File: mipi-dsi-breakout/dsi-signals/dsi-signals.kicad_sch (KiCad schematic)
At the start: 19 parts, among them J1 Conn_01x03_Pin, J2 Conn_01x06_Pin, J5 Conn_01x01_Pin

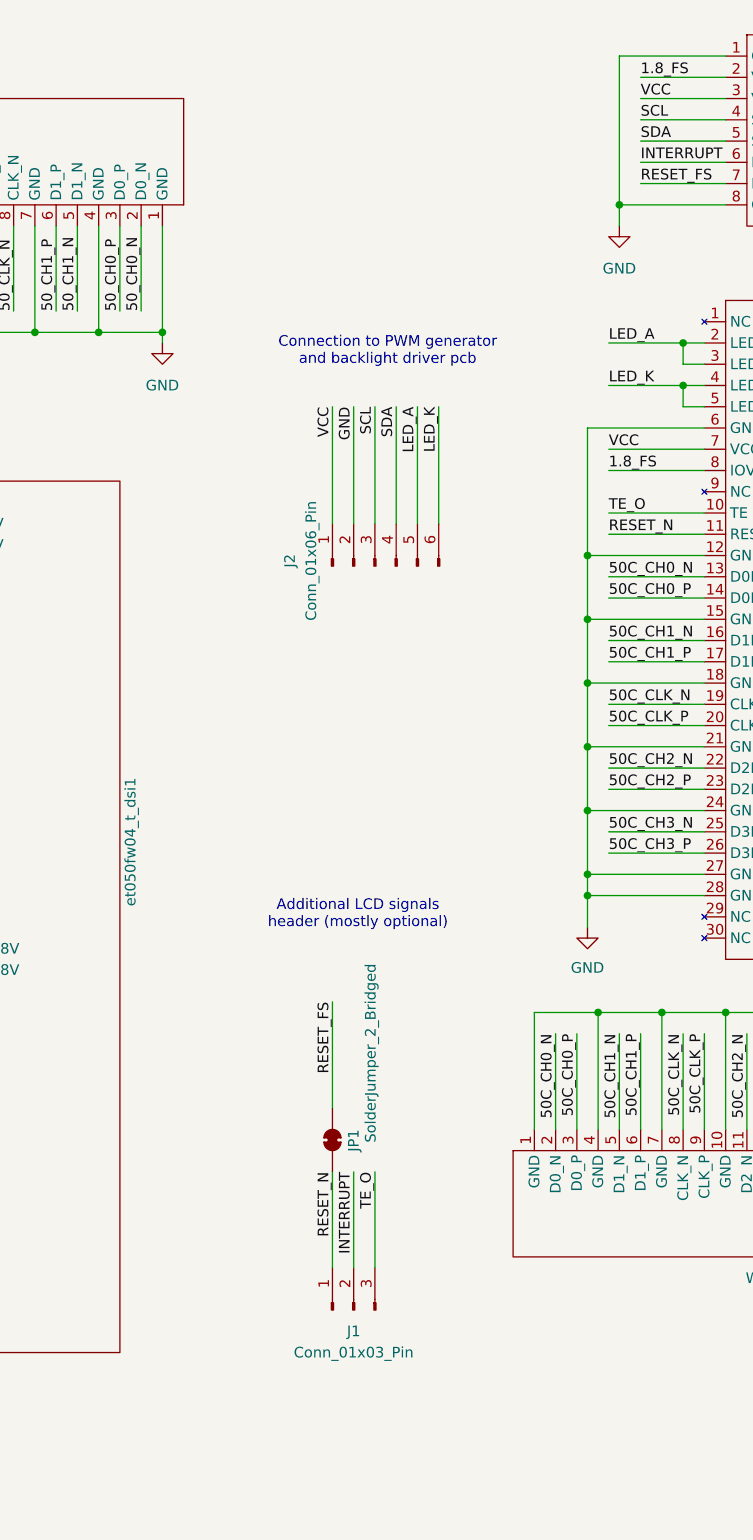
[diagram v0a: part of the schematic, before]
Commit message: Add SUS grounding to dsi-signals. Add lcd-peripherals.
To the mipi-dsi-breakout project.
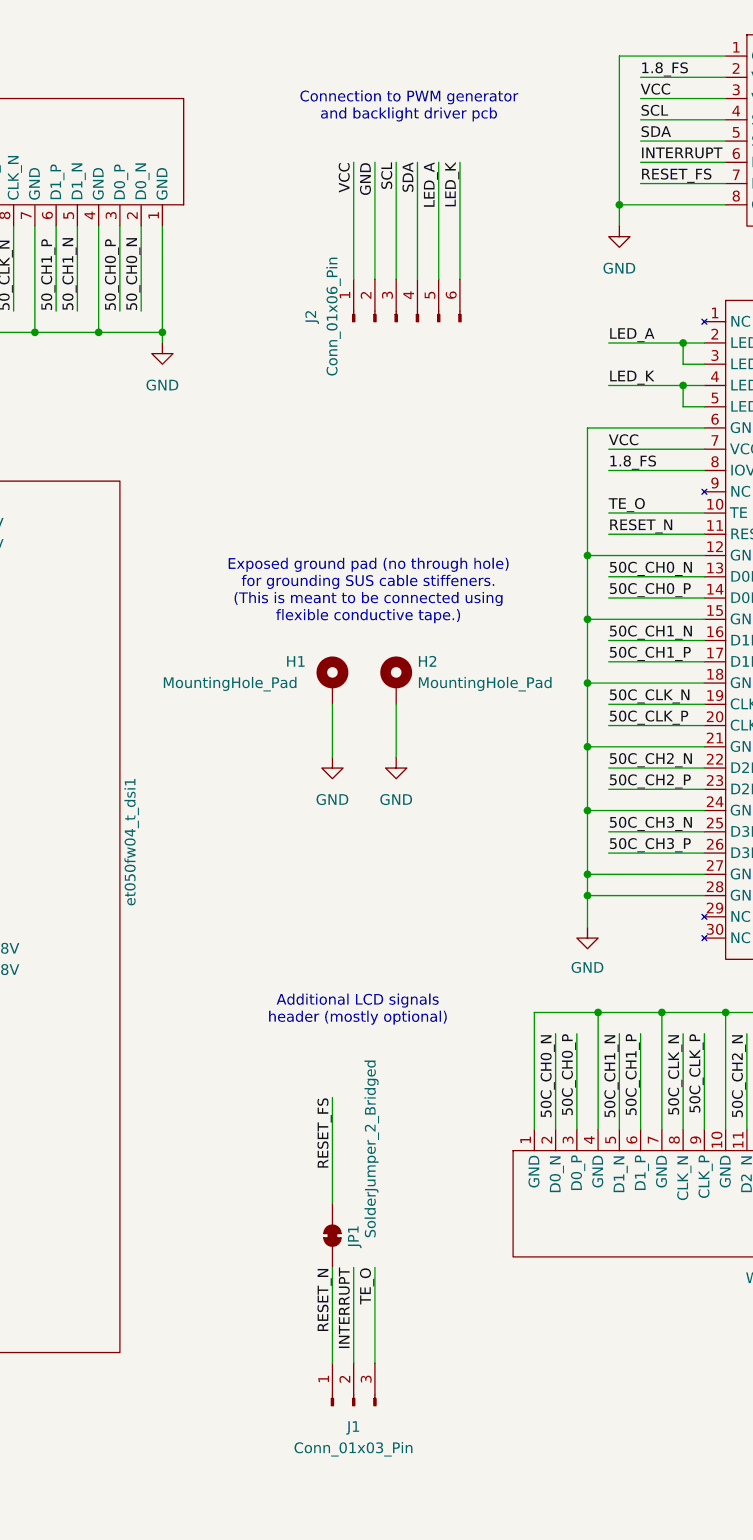
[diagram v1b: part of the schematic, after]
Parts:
- added H1, H2: MountingHole_Pad, symbol Mechanical:MountingHole_Pad
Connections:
- net GND: now also H1.1, H2.1
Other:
- note added: "Exposed ground pad (no through hole) for grounding SUS cable stiffeners. (This is meant to be connected using flexible conductive tape.)"
- moved on the sheet: J1, J2, JP1

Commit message: First draft of dsi signal routing in mipi dsi breakout.
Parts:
- H1, H2: footprint (none) -> project:sus-grounding-pad
- J1: footprint (none) -> Connector_PinHeader_2.54mm:PinHeader_1x03_P2.54mm_Vertical
- J2: footprint (none) -> Connector_PinHeader_2.54mm:PinHeader_1x06_P2.54mm_Vertical
- J5: footprint (none) -> Connector_PinHeader_2.54mm:PinHeader_1x01_P2.54mm_Vertical
- JP1, JP2: footprint (none) -> Jumper:SolderJumper-2_P1.3mm_Bridged_Pad1.0x1.5mm
- R1, R2, R3, R4: footprint (none) -> Resistor_SMD:R_0805_2012Metric
- W1, W2, W3, W4: footprint (none) -> project:Cvilux_CF4222FH0R0-05-NH_22pos-0.5mm-zif
- et050fw04_t_dsi1: footprint (none) -> project:Cvilux_CF4240FH0R0-05-NH_40pos-0.5mm-zif
- et060hd02_t_dsi1: footprint (none) -> project:Cvilux_CF5825DH0RA-NH_25pos-0.3mm-zif
- tst043wvbi_130c_ctp1: footprint (none) -> project:TE_1-2328702-0_10pos-0.5mm-zif
- tst043wvbi_130c_dsi1: footprint (none) -> project:Cvilux_CF4220FH0R0-05-NH_20pos-0.5mm-zif
- tst050hdbs_80c_ctp1: footprint (none) -> project:TE_2328702_8pos-0.5mm-zif
- tst050hdbs_80c_dsi1: footprint (none) -> project:Cvilux_CF4230FH0R0-05-NH_30pos-0.5mm-zif
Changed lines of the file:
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@@
 			)
 		)
-		(property "Footprint" ""
+		(property "Footprint" "project:Cvilux_CF4222FH0R0-05-NH_22pos-0.5mm-zif"
 			(at 53.34 181.61 0)
 			(effects
@@
 			)
 		)
-		(property "Footprint" ""
+		(property "Footprint" "project:Cvilux_CF4230FH0R0-05-NH_30pos-0.5mm-zif"
 			(at 210.82 85.09 0)
 			(effects
@@
 			)
 		)
-		(property "Footprint" ""
+		(property "Footprint" "Resistor_SMD:R_0805_2012Metric"
 			(at 71.882 151.13 90)
 			(effects
@@
 			)
 		)
-		(property "Footprint" ""
+		(property "Footprint" "Resistor_SMD:R_0805_2012Metric"
 			(at 76.962 151.13 90)
 			(effects
@@
 			)
 		)
-		(property "Footprint" ""
+		(property "Footprint" "Jumper:SolderJumper-2_P1.3mm_Bridged_Pad1.0x1.5mm"
 			(at 156.21 157.48 0)
 			(effects
@@
 			)
 		)
-		(property "Footprint" ""
+		(property "Footprint" "Connector_PinHeader_2.54mm:PinHeader_1x06_P2.54mm_Vertical"
 			(at 163.83 48.26 0)
 			(effects
@@
 			)
 		)
-		(property "Footprint" ""
+		(property "Footprint" "project:sus-grounding-pad"
 			(at 163.83 91.44 0)
 			(effects
@@
 			)
 		)
-		(property "Footprint" ""
+		(property "Footprint" "project:sus-grounding-pad"
 			(at 156.21 91.44 0)
 			(effects
@@
 			)
 		)
-		(property "Footprint" ""
+		(property "Footprint" "project:Cvilux_CF4222FH0R0-05-NH_22pos-0.5mm-zif"
 			(at 109.22 27.94 0)
 			(effects
@@
 			)
 		)
-		(property "Footprint" ""
+		(property "Footprint" "project:Cvilux_CF4220FH0R0-05-NH_20pos-0.5mm-zif"
 			(at 53.34 124.46 0)
 			(effects
@@
 			)
 		)
-		(property "Footprint" ""
+		(property "Footprint" "project:Cvilux_CF4222FH0R0-05-NH_22pos-0.5mm-zif"
 			(at 254 26.67 0)
 			(effects
@@
 			)
 		)
-		(property "Footprint" ""
+		(property "Footprint" "project:Cvilux_CF4240FH0R0-05-NH_40pos-0.5mm-zif"
 			(at 120.65 105.41 0)
 			(effects
@@
 			)
 		)
-		(property "Footprint" ""
+		(property "Footprint" "Jumper:SolderJumper-2_P1.3mm_Bridged_Pad1.0x1.5mm"
 			(at 35.56 26.67 0)
 			(effects
@@
 			)
 		)
-		(property "Footprint" ""
+		(property "Footprint" "Resistor_SMD:R_0805_2012Metric"
 			(at 225.552 123.19 90)
 			(effects
@@
 			)
 		)
-		(property "Footprint" ""
+		(property "Footprint" "project:TE_1-2328702-0_10pos-0.5mm-zif"
 			(at 55.88 73.66 0)
 			(effects
@@
 			)
 		)
-		(property "Footprint" ""
+		(property "Footprint" "Connector_PinHeader_2.54mm:PinHeader_1x03_P2.54mm_Vertical"
 			(at 158.75 177.8 0)
 			(effects
@@
 			)
 		)
-		(property "Footprint" ""
+		(property "Footprint" "project:Cvilux_CF4222FH0R0-05-NH_22pos-0.5mm-zif"
 			(at 207.01 153.67 0)
 			(effects
@@
 			)
 		)
-		(property "Footprint" ""
+		(property "Footprint" "project:TE_2328702_8pos-0.5mm-zif"
 			(at 210.82 25.4 0)
 			(effects
@@
 			)
 		)
-		(property "Footprint" ""
+		(property "Footprint" "Connector_PinHeader_2.54mm:PinHeader_1x01_P2.54mm_Vertical"
 			(at 57.15 26.67 0)
 			(effects
@@
 			)
 		)
-		(property "Footprint" ""
+		(property "Footprint" "Resistor_SMD:R_0805_2012Metric"
 			(at 230.632 123.19 90)
 			(effects
@@
 			)
 		)
-		(property "Footprint" ""
+		(property "Footprint" "project:Cvilux_CF5825DH0RA-NH_25pos-0.3mm-zif"
 			(at 273.05 97.79 0)
 			(effects
